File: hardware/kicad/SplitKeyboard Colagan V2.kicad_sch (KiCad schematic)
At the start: 31 parts, among them J1 USB_C_Receptacle_PowerOnly_6P

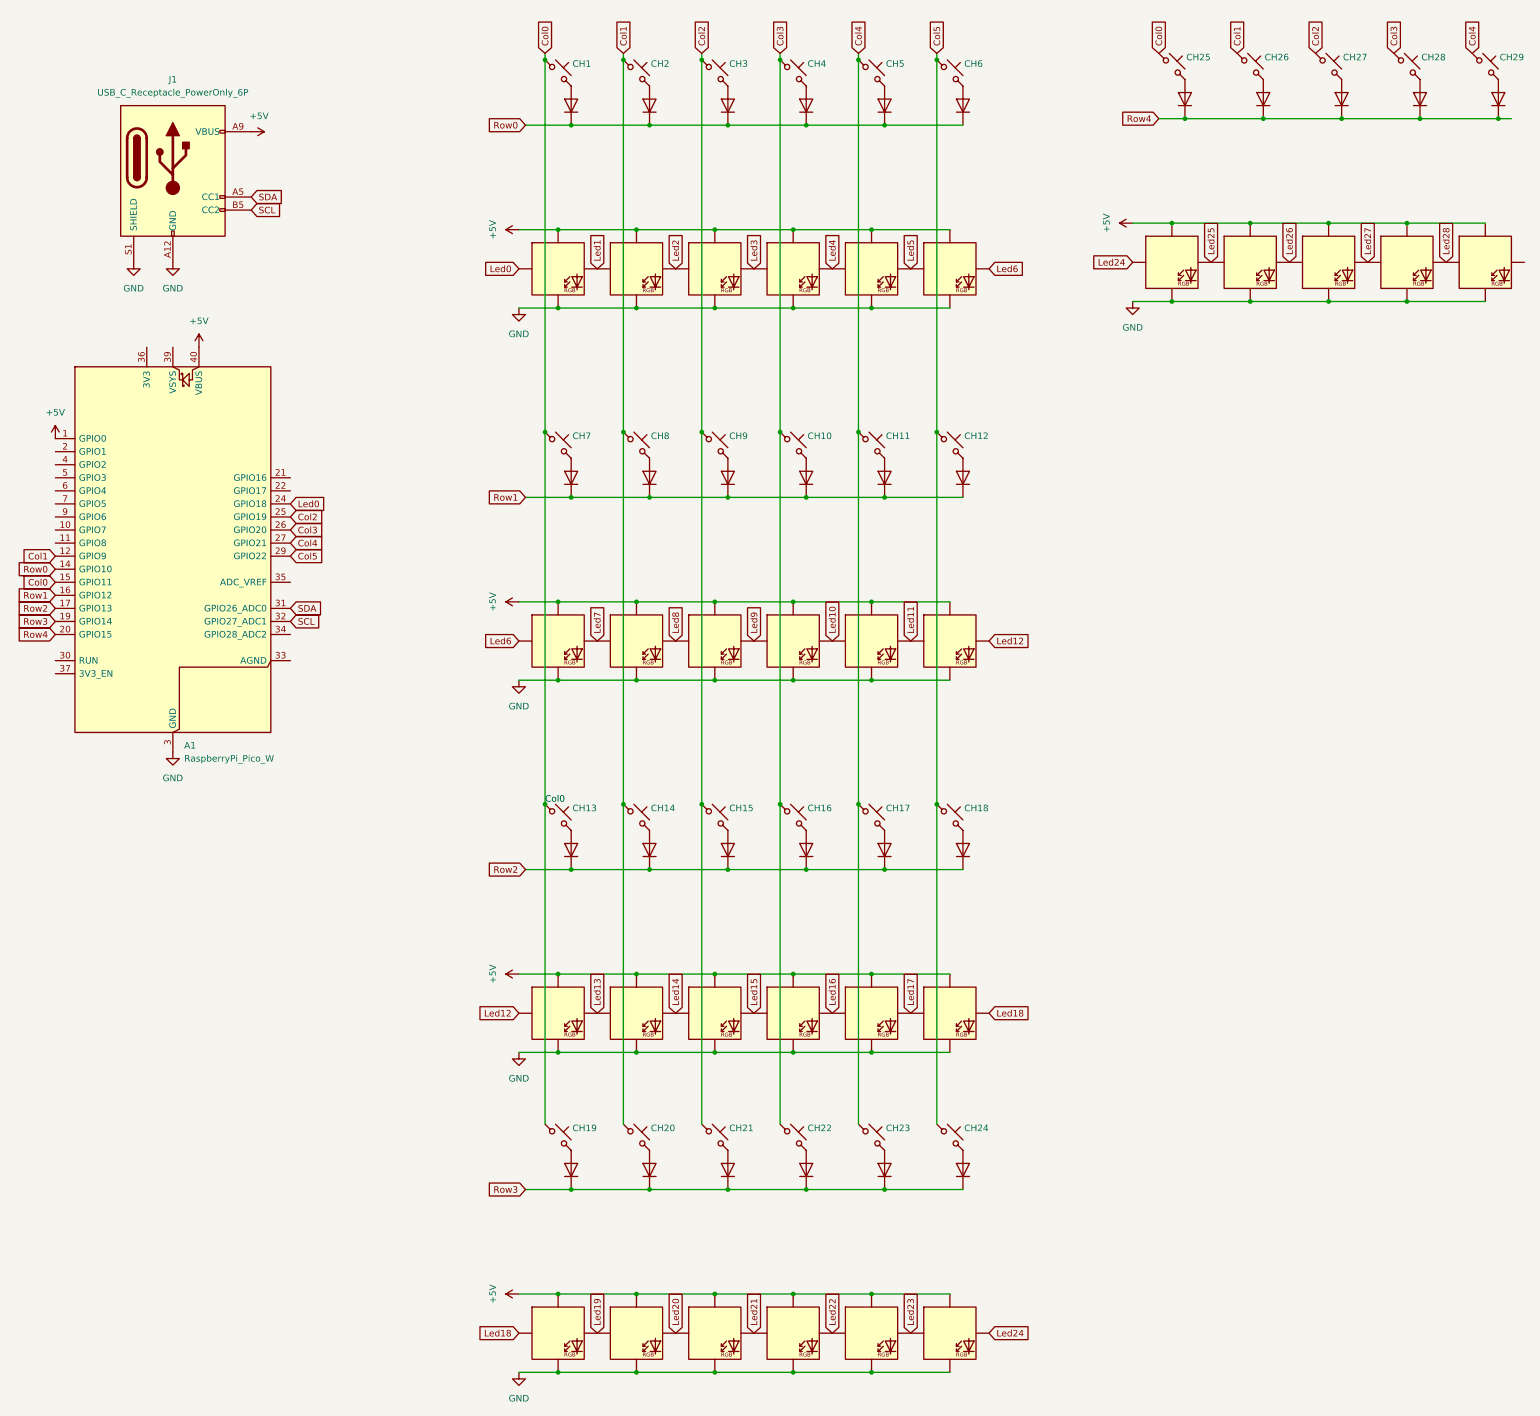
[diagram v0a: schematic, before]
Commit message: chore: replace hardware sources with the fabricated V2 PCB
Archive the old 20/10/2025 revision outside the repo, add the V2 KiCad
project and library, and regenerate the renders with kicad-cli.

Co-Authored-By: Claude Sonnet 5.5 <noreply@anthropic.com>
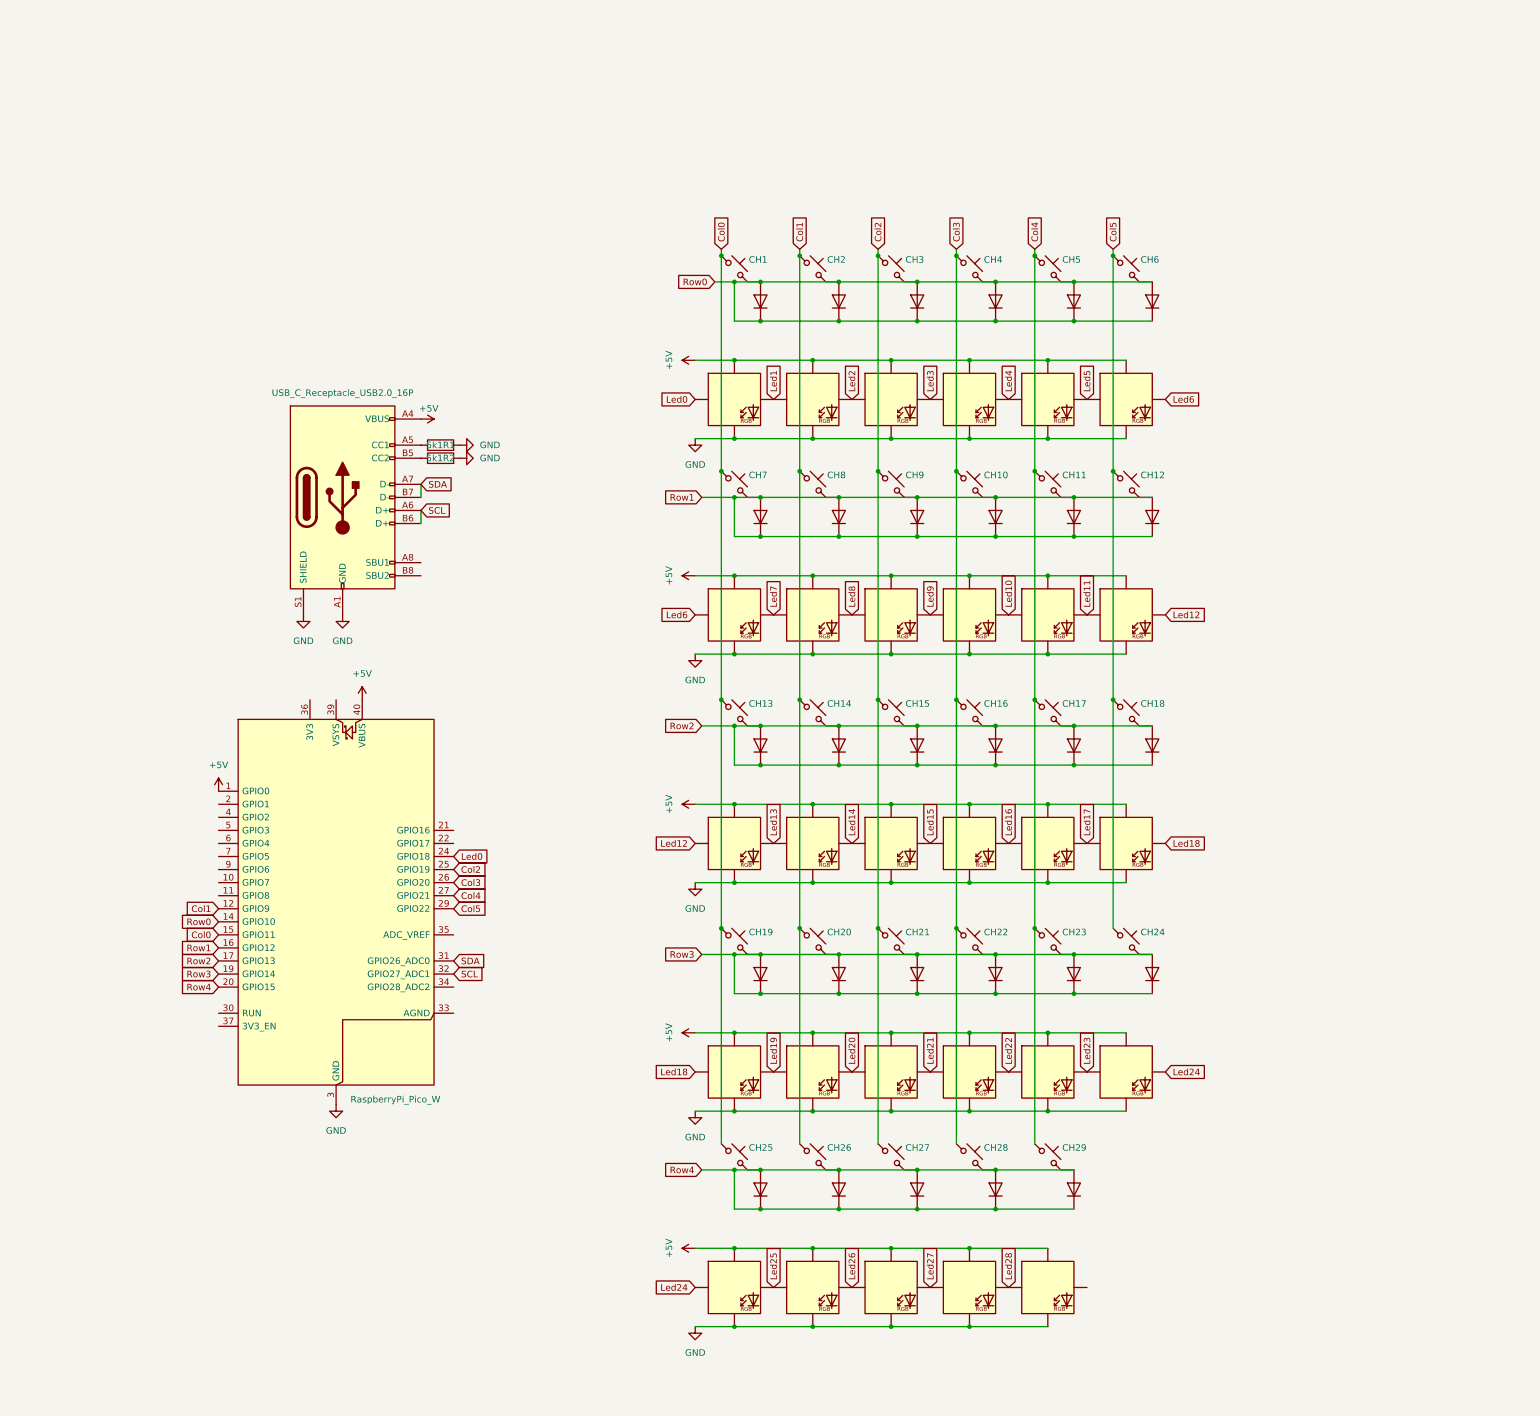
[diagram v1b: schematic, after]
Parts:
- removed J1: USB_C_Receptacle_PowerOnly_6P, Library SplitKeyboard Colagan:USB_C_6P_Colagan, symbol Connector:USB_C_Receptacle_PowerOnly_6P
- added 5k1R1: R1, Library SplitKeyboard Colagan:Capasitor_SMD_1206_Reversible_ColaganV3, symbol Device:R
- added 5k1R2: ~, Library SplitKeyboard Colagan:Capasitor_SMD_1206_Reversible_ColaganV3, symbol Device:R
- added J2: USB_C_Receptacle_USB2.0_16P, Library SplitKeyboard Colagan:USB_C_16P-Reversible-colagan, symbol Connector:USB_C_Receptacle_USB2.0_16P
- CH1, CH10, CH11, CH13, CH14, CH15, CH16, CH17, CH19, CH2, CH20, CH21, CH22, CH23, CH25, CH26, CH27, CH28, CH29, CH3, CH4, CH5, CH7, CH8, CH9: footprint Library SplitKeyboard Colagan:KS33-HS-Colagan-1U-Reverse-REF4 -> Library SplitKeyboard Colagan:KS33-HS-Colagan-1U-Final; symbol Colagan:KS33_SW_HS_Colagan_V2_Fix2 -> Colagan:KS33_SW_HS_Colagan_V3
- CH12, CH6: footprint Library SplitKeyboard Colagan:KS33-HS-Colagan-1.5U-Reverse-REF4 -> Library SplitKeyboard Colagan:KS33-HS-Colagan-1.5U-Final; symbol Colagan:KS33_SW_HS_Colagan_V2_1.5U -> Colagan:KS33_SW_HS_Colagan_V3
- CH18, CH24: footprint Library SplitKeyboard Colagan:KS33-HS-Colagan-1.5U-Reverse-REF4 -> Library SplitKeyboard Colagan:KS33-HS-Colagan-1.5U-Final; symbol Colagan:KS33_SW_HS_Colagan_V2_Fix2 -> Colagan:KS33_SW_HS_Colagan_V3
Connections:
- net +5V: now also J2.A4 (VBUS), J2.A9 (VBUS), J2.B4 (VBUS), J2.B9 (VBUS)
- net GND: now also 5k1R1.2, 5k1R2.2, J2.A1 (GND), J2.A12 (GND), J2.B1 (GND), J2.B12 (GND), J2.S1 (SHIELD)
- net Row0: now also CH1.2, CH2.2, CH3.2, CH4.2, CH5.2, CH6.2
- net Row1: now also CH10.2, CH11.2, CH12.2, CH7.2, CH8.2, CH9.2
- net Row2: now also CH13.2, CH14.2, CH15.2, CH16.2, CH17.2, CH18.2
- net Row3: now also CH19.2, CH20.2, CH21.2, CH22.2, CH23.2, CH24.2
- net Row4: now also CH25.2, CH26.2, CH27.2, CH28.2, CH29.2
- net SCL: now also J2.A6 (D+), J2.B6 (D+)
- net SDA: now also J2.A7 (D-), J2.B7 (D-)
- new net: 5k1R1.1, J2.A5 (CC1)
- new net: 5k1R2.1, J2.B5 (CC2)
